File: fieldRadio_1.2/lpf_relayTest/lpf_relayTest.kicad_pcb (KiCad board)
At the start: 2 copper layers, 71 parts, among them J1 Conn_Coaxial_Small, J2 Conn_Coaxial_Small, J3 Conn_Coaxial_Small, J4 Conn_Coaxial_Small, J5 Conn_01x02, J6 Conn_01x02, J7 Conn_01x02, J8 Conn_01x02, K1 G6SU-2, K2 G6SU-2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

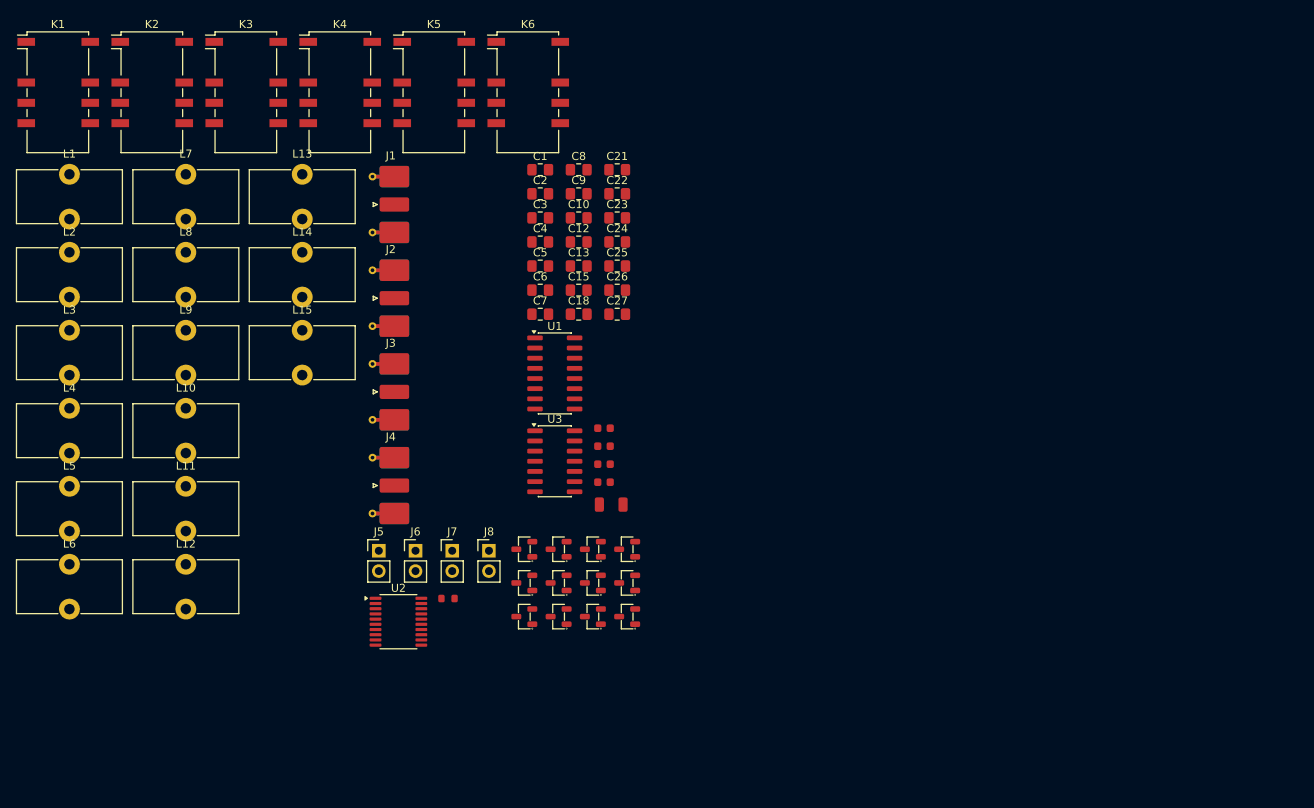
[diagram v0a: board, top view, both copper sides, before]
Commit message: completed first pass placement.
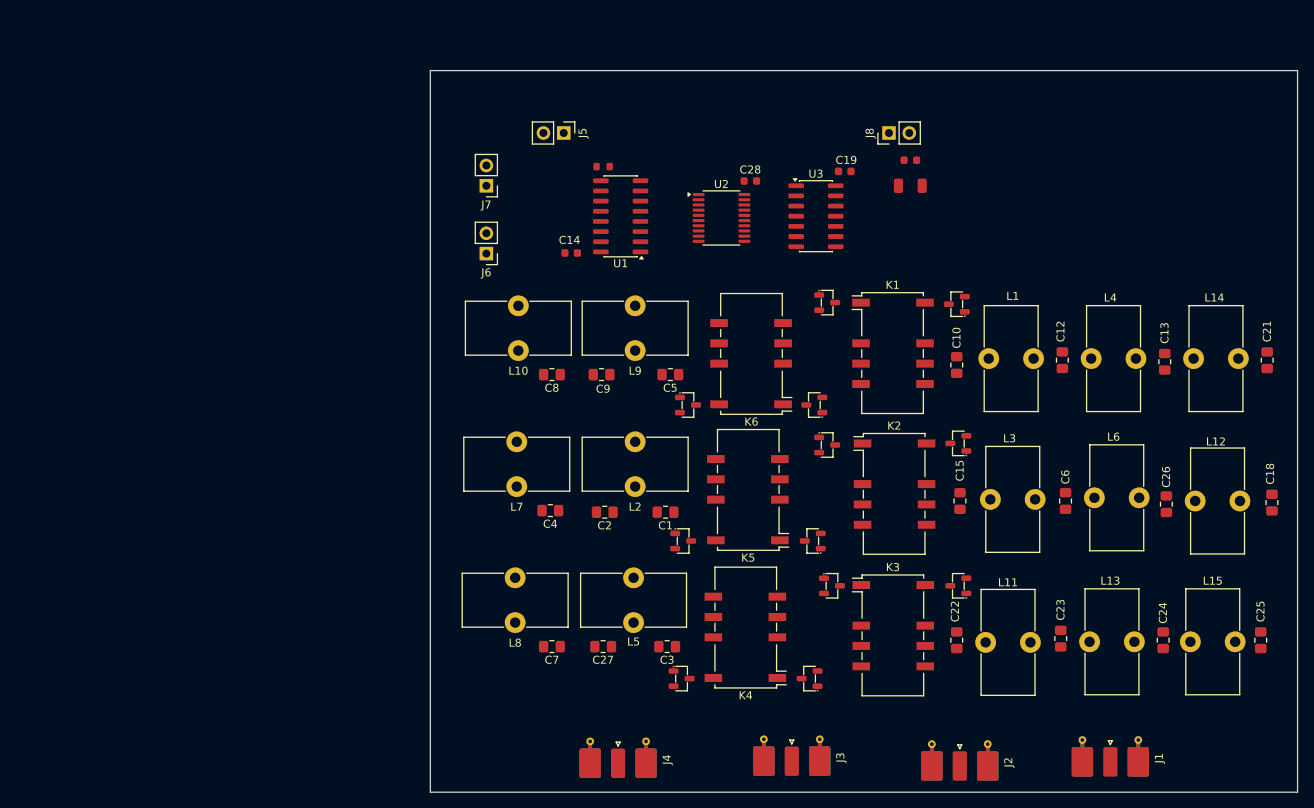
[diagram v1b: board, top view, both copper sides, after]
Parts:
- moved L6 128.4 mm to (172.8, 92.0), turned to 90 degrees
- moved L4 127.9 mm to (172.4, 74.6), turned to 90 degrees
- moved L12 126.4 mm to (185.4, 92.4), turned to 90 degrees
- moved L15 117.6 mm to (184.8, 110.0), turned to 90 degrees
- moved L1 117.2 mm to (159.6, 74.6), turned to 90 degrees
- moved L3 117.0 mm to (159.8, 92.2), turned to 90 degrees
- moved L13 114.5 mm to (172.2, 110.0), turned to 90 degrees
- moved J1 113.4 mm to (174.8, 125.3), turned to -90 degrees
- moved L14 112.2 mm to (185.2, 74.6), turned to 90 degrees
- moved K1 109.3 mm to (147.6, 74.0)
- moved K3 105.6 mm to (147.7, 109.3)
- moved K2 105.5 mm to (147.8, 91.6)
- moved L11 101.9 mm to (159.2, 110.1), turned to 90 degrees
- moved C25 93.1 mm to (193.6, 109.8), turned to -90 degrees
- moved J2 91.7 mm to (156.0, 125.8), turned to -90 degrees
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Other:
- board outline added: 108.4 x 90.2 mm

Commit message: working on layout of relayTest
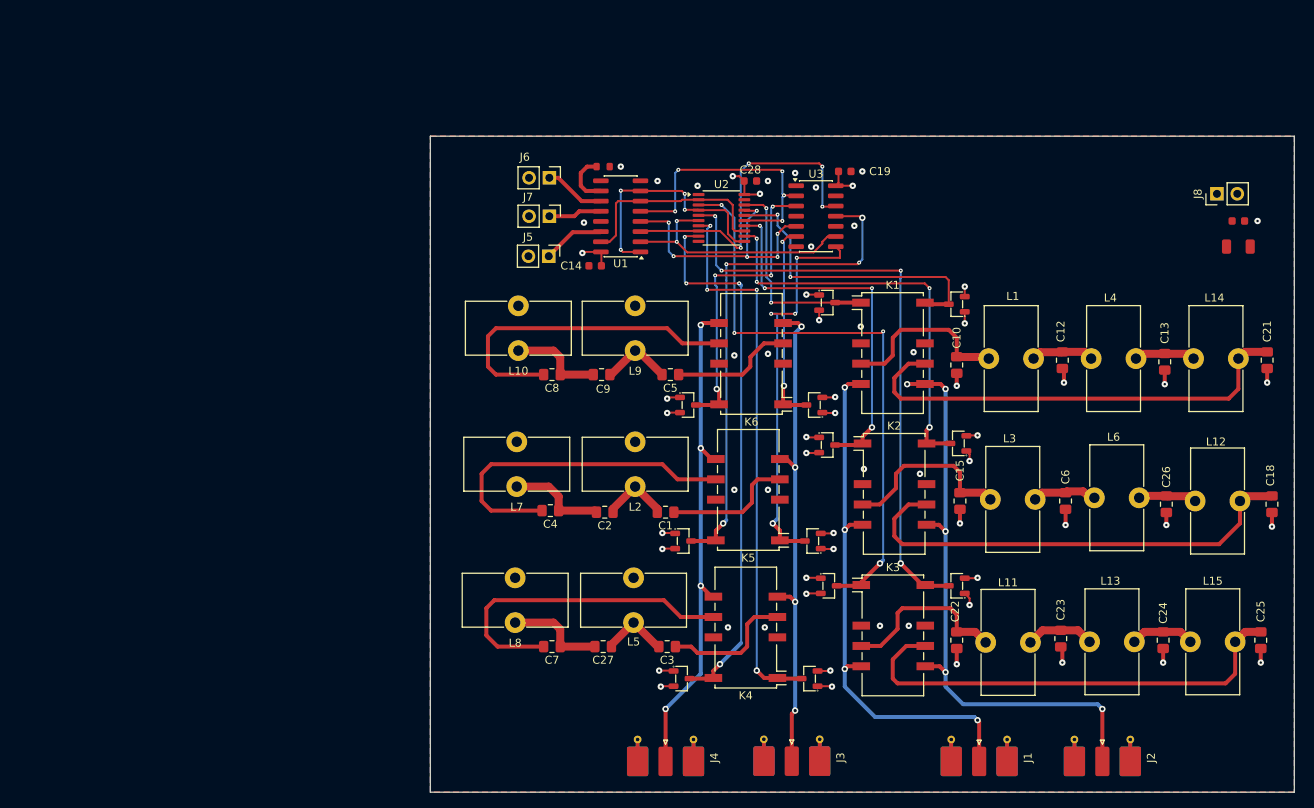
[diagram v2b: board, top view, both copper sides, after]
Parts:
- moved C11 41.7 mm to (190.8, 57.4)
- moved C16 41.7 mm to (190.8, 60.6)
- moved J8 41.7 mm to (188.1, 54.0)
- moved J2 17.8 mm to (173.8, 125.2)
- moved J1 16.4 mm to (158.4, 125.2)
- moved D5 16.2 mm to (139.6, 103.0), turned to 180 degrees
- moved D6 15.6 mm to (155.6, 103.0), turned to 0 degrees
- moved J5 15.5 mm to (104.6, 61.8)
- moved J6 12.3 mm to (104.7, 52.0), turned to -90 degrees
- moved J7 8.74 mm to (104.7, 56.8), turned to -90 degrees
- moved J4 5.94 mm to (119.2, 125.2)
- moved C14 3.40 mm to (110.4, 63.0)
- moved C18 0.20 mm to (195.0, 92.8)
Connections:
- net Net-(U1-QA) renamed /QA
- net Net-(U1-QB) renamed /QB
- net Net-(U1-QC) renamed /QC
- net Net-(U1-QD) renamed /QD
- net Net-(U1-QE) renamed /QE
- net Net-(U1-QF) renamed /QF
- K3 pad 12: /LP1517M+ -> /LP1517M-
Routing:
- net /LP1517M-: track 0.00 -> 75.6 mm, vias 0 -> 4
- net LPOUT: track 0.00 -> 75.1 mm, vias 0 -> 5
- net /LP1517M+: track 0.00 -> 74.2 mm, vias 0 -> 4
- net /HP40M+: track 0.00 -> 69.5 mm, vias 0 -> 4
- net /HP40M-: track 0.00 -> 68.1 mm, vias 0 -> 4
- net LPIN: track 0.00 -> 67.9 mm, vias 0 -> 4
- net /HP2030M-: track 0.00 -> 64.0 mm, vias 0 -> 4
- net HPOUT: track 0.00 -> 63.4 mm, vias 0 -> 4
- net HPIN: track 0.00 -> 62.2 mm, vias 0 -> 4
- net Net-(C18-Pad1): track 0.00 -> 58.7 mm
- net Net-(C25-Pad1): track 0.00 -> 58.4 mm
- net Net-(C21-Pad1): track 0.00 -> 57.9 mm
- net /LP2030M-: track 0.00 -> 51.6 mm, vias 0 -> 4
- net /HP2030M+: track 0.00 -> 49.9 mm, vias 0 -> 4
- net /LP2030M+: track 0.00 -> 46.8 mm, vias 0 -> 4
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- added copper zone on In2.Cu, net /VDD5_RELAY
- added copper zone on B.Cu, net GND
- added copper zone on F.Cu, net GND
- added copper zone on In1.Cu, net GND
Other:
- board size 108.4 x 90.2 mm -> 108 x 82 mm
- copper layers 2 -> 4

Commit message: Relay Boarc Layout complete
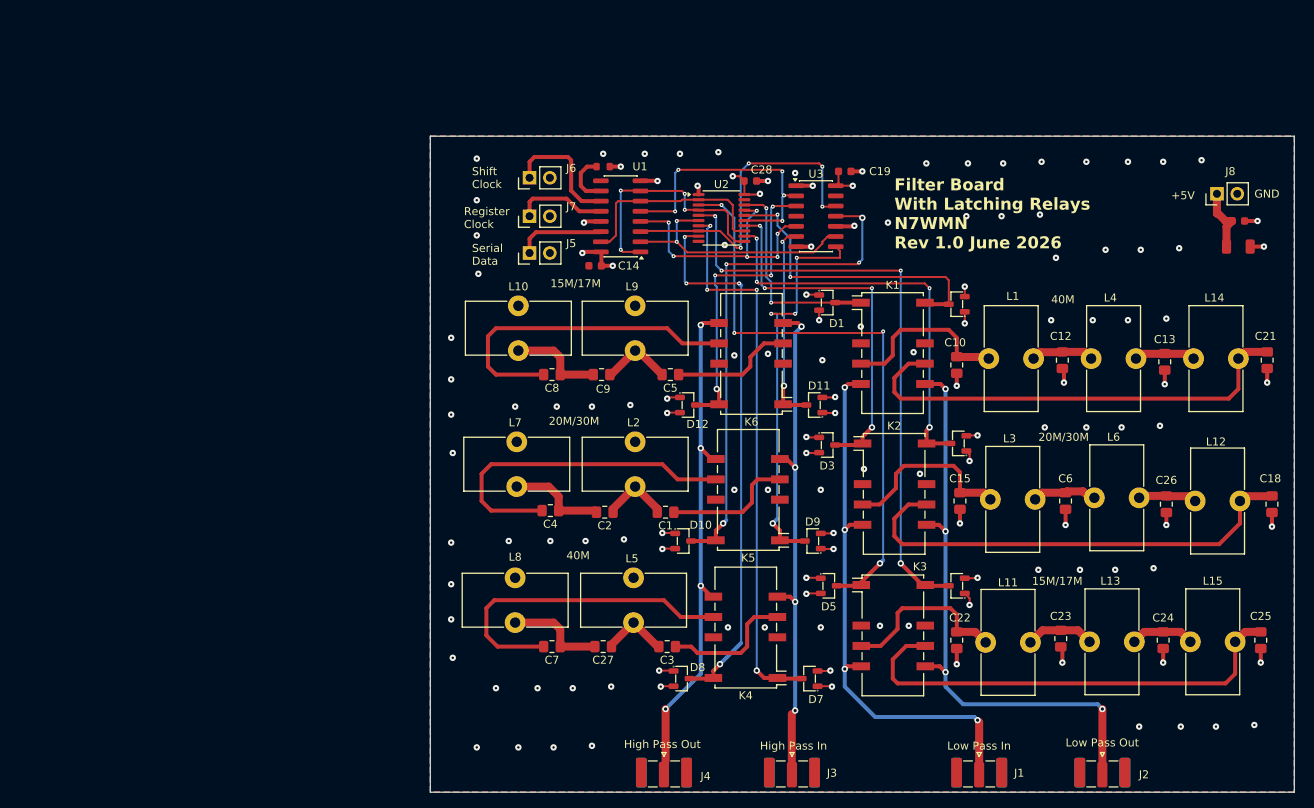
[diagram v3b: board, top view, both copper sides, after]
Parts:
- J1, J2, J3, J4: footprint Connector_Coaxial:SMA_Molex_73251-2120_EdgeMount_Horizontal -> Connector_Coaxial:SMA_Samtec_SMA-J-P-H-ST-EM1_EdgeMount
- moved J6 2.47 mm to (102.2, 52.0), turned to 90 degrees
- moved J7 2.47 mm to (102.2, 56.8), turned to 90 degrees
- moved J5 2.43 mm to (102.2, 61.4), turned to 90 degrees
- moved J3 1.43 mm to (135.0, 126.6)
- moved J4 1.41 mm to (119.0, 126.6)
- moved J1 1.40 mm to (158.4, 126.6)
- moved J2 1.40 mm to (173.8, 126.6)
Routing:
- net GND: track 41.3 -> 59.3 mm, vias 46 -> 115
- net /VDD5_RELAY: track 32.3 -> 43.4 mm, vias 17 -> 18
- net Net-(J6-Pin_1): track 7.65 -> 15.7 mm
- net Net-(J7-Pin_1): track 6.69 -> 11.5 mm
- net Net-(J5-Pin_1): track 7.79 -> 11.1 mm
- net LPOUT: track 75.1 -> 72.9 mm, vias 5 -> 4
- added copper zone on In2.Cu, net GND
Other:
- board text added: "+5V"
- board text added: "15M/17M"
- board text added: "20M/30M"
- board text added: "40M"
- board text added: "Filter Board With Latching Relays N7WMN Rev 1.0 June 2026"
- board text added: "GND"
- board text added: "High Pass In"
- board text added: "High Pass Out"
- board text added: "Low Pass In"
- board text added: "Low Pass Out"
- board text added: "Register Clock"
- board text added: "Serial Data"
- board text added: "Shift Clock"
